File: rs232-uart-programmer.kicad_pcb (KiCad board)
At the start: 2 copper layers, 78.5 x 67.2 mm, 49 parts, among them J1 DB9_Female_MountingHoles, J2 Barrel_Jack, J3 Conn_01x03_Male, J4 Conn_01x02_Male, J5 USB_B, J6 Conn_01x05_Male, Q1 2N3905, Q2 AO3407A, Q3 2N3905, U1 L7805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

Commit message: Added Silkscreen description
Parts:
- removed the ? at (52.2, 105.2)
- removed the ? at (53.0, 44.8)
- added ?: MountingHole_3mm, MountingHole:MountingHole_3mm, F.Cu at (52.5, 104.8)
- added ?: MountingHole_3mm, MountingHole:MountingHole_3mm, F.Cu at (52.8, 45.0)
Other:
- board text added: "Isolated RS232 to UART Designed by DarkMagus"
- board text added: "JLCJLCJLCJLC"
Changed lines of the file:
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@@
   (general
     (thickness 1.6)
-    (drawings 4)
+    (drawings 7)
     (tracks 215)
     (zones 0)
@@
   )
   (module MountingHole:MountingHole_3mm (layer F.Cu)
-    (at 52.25 105.25)
+    (at 52.5 104.75)
     (descr "Mounting Hole 3mm, no annular")
     (tags "mounting hole 3mm no annular")
@@
   )
   (module MountingHole:MountingHole_3mm (layer F.Cu)
-    (at 53 44.75)
+    (at 52.75 45)
     (descr "Mounting Hole 3mm, no annular")
     (tags "mounting hole 3mm no annular")
@@
     (pad 1 thru_hole circle (at 0 0 90) (size 1.5 1.5) (drill 1) (layers *.Cu *.Mask F.SilkS)
       (net 9 "Net-(C9-Pad1)"))
+    (model ${KIPRJMOD}/B0505LS-1WR3.step
+      (offset (xyz 7.5 -2 0))
+      (scale (xyz 1 1 1))
+      (rotate (xyz -90 0 0))
+    )
   )
   (module Diode_THT:D_DO-35_SOD27_P7.62mm_Horizontal (layer F.Cu)
@@
     (pad 1 np_thru_hole circle (at 0 0) (size 3 3) (drill 3) (layers *.Cu *.Mask))
   )
+  (gr_text "Isolated RS232 to UART\nDesigned by DarkMagus" (at 72.75 44.25) (layer F.SilkS)
+    (effects (font (size 1.5 1.5) (thickness 0.3)))
+  )
+  (gr_text JLCJLCJLCJLC (at 37.25 89.25 90) (layer F.SilkS)
+    (effects (font (size 1.5 1.5) (thickness 0.3)))
+  )
+  (gr_text "Isolated RS232 to UART\nDesigned by DarkMagus" (at 72.75 44.25) (layer B.SilkS)
+    (effects (font (size 1.5 1.5) (thickness 0.3)) (justify mirror))
+  )
   (gr_line (start 34 108.5) (end 34 41.25) (layer Edge.Cuts) (width 0.2))

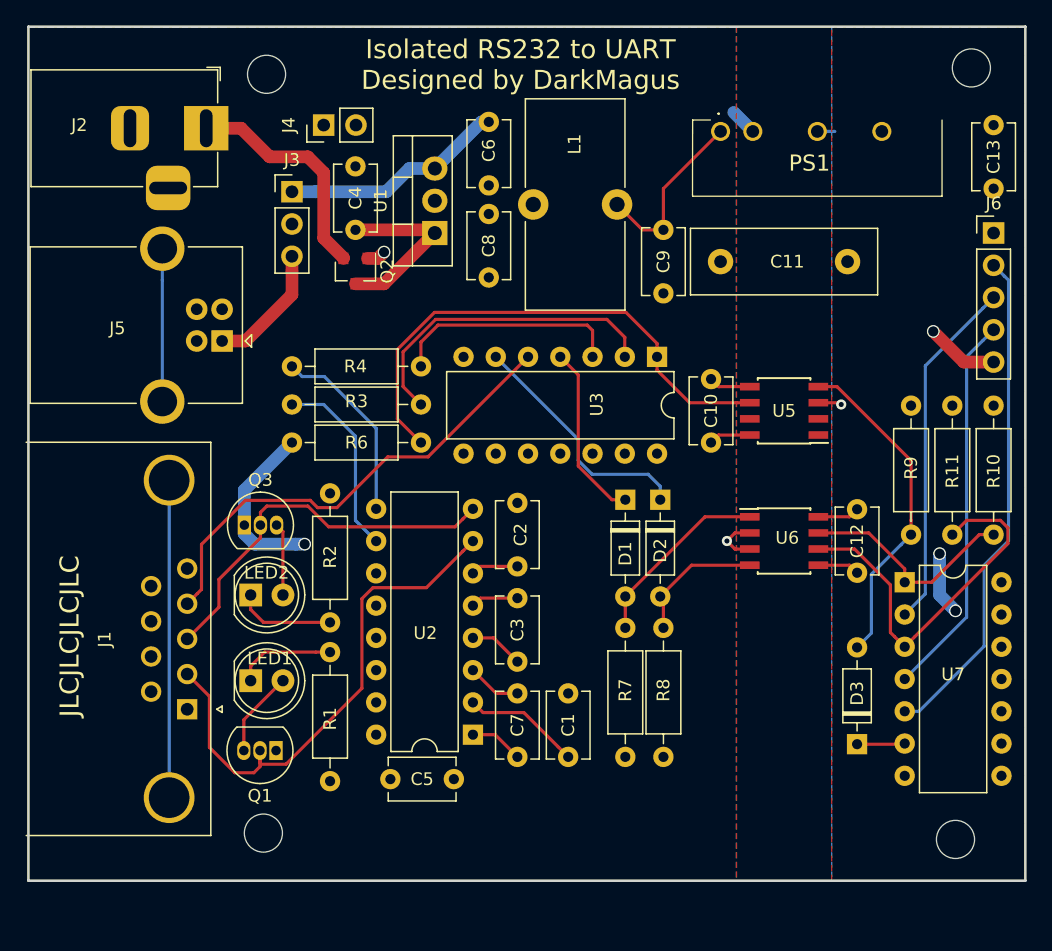
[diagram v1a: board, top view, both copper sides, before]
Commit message: Added mounting holes
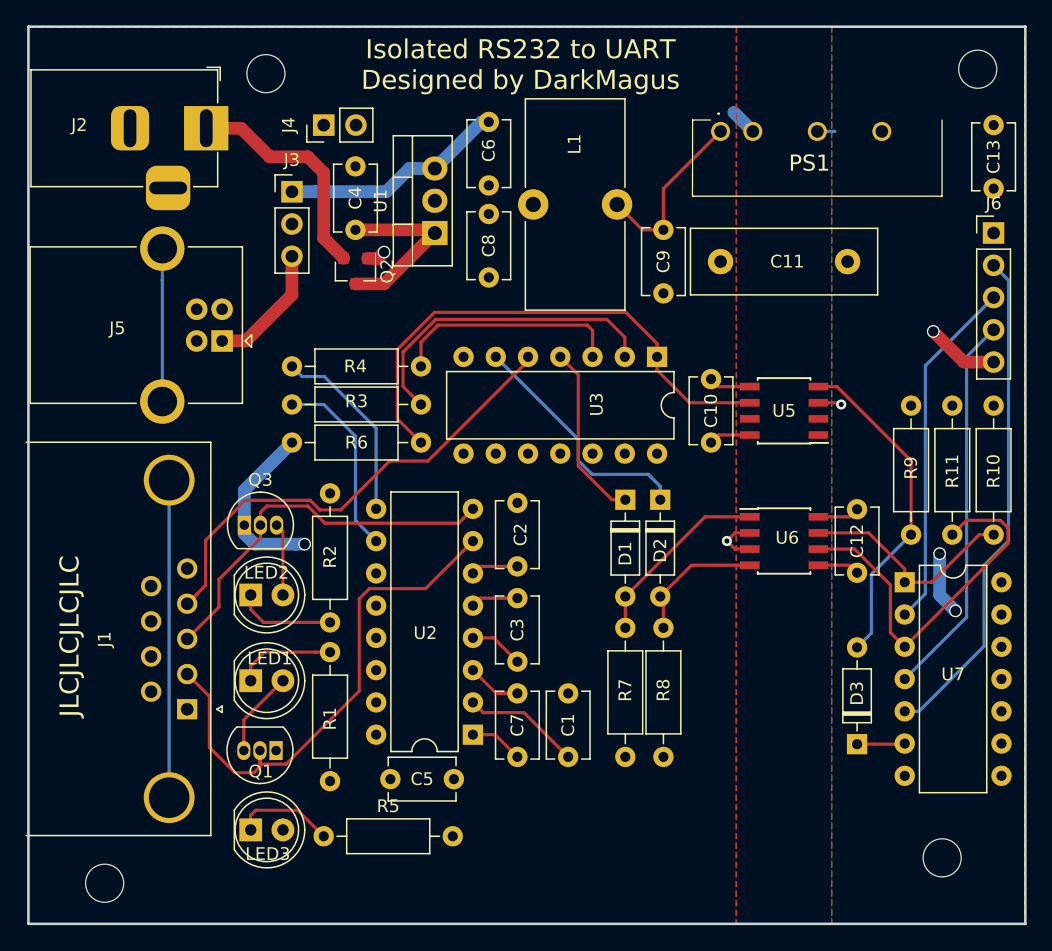
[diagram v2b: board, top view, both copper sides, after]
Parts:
- removed ? (x4): MountingHole_3mm, MountingHole:MountingHole_3mm
- added H1: MountingHole, MountingHole:MountingHole_3mm, F.Cu at (106.0, 106.7)
- added H2: MountingHole, MountingHole:MountingHole_3mm, F.Cu at (108.8, 44.6)
- added H3: MountingHole, MountingHole:MountingHole_3mm, F.Cu at (40.0, 108.7)
- added H4: MountingHole, MountingHole:MountingHole_3mm, F.Cu at (52.7, 45.0)
- added LED3: LED, LED_THT:LED_D5.0mm, F.Cu at (51.5, 104.5)
- added R5: 220, Resistor_THT:R_Axial_DIN0207_L6.3mm_D2.5mm_P10.16mm_Horizontal, F.Cu at (57.2, 105.0)
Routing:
- net Net-(LED3-Pad1): track 0.00 -> 7.91 mm
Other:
- board size 78.5 x 67.2 mm -> 78.5 x 70.7 mm
